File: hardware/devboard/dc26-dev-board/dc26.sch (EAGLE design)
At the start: 112 parts, among them CN1 JST, IC3 LDL112D33R, J1 DC26 Shitty AddOn, J2 DC26 Shitty AddOn, P1 SPDT_SSAJ120100, Y1 ABL-8.000MHZ-B2

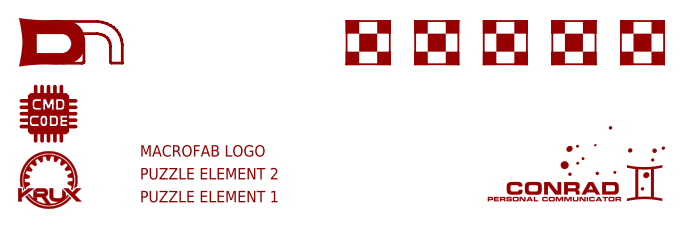
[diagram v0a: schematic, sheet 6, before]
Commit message: basics of sd card working still have work todo to get flatbuffers working Buttons now working
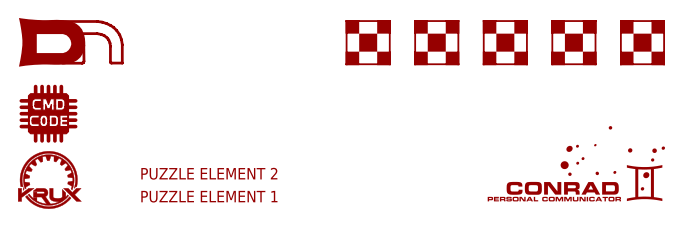
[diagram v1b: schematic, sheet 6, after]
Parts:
- removed U$12: MACROFAB_LOGO, darknet_parts_library:MACROFAB_LOGO
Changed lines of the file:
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@@
 <?xml version="1.0" encoding="utf-8"?>
 <!DOCTYPE eagle SYSTEM "eagle.dtd">
-<eagle version="7.7.0">
+<eagle version="9.0.1">
 <drawing>
 <settings>
 <setting alwaysvectorfont="no"/>
+<setting keepoldvectorfont="yes"/>
 <setting verticaltext="up"/>
 </settings>
@@
 <part name="U$10" library="darknet_parts_library" deviceset="FIDUCIAL_DN" device="CORNER"/>
 <part name="U$11" library="darknet_parts_library" deviceset="FIDUCIAL_DN" device="CORNER"/>
-<part name="U$12" library="darknet_parts_library" deviceset="MACROFAB_LOGO" device=""/>
 </parts>
 <sheets>
@@
 <instance part="U$10" gate="G$1" x="45.72" y="15.24"/>
 <instance part="U$11" gate="G$1" x="38.1" y="15.24"/>
-<instance part="U$12" gate="G$1" x="15.24" y="5.08"/>
 </instances>
 <busses>
